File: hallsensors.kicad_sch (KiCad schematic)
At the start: 23 parts

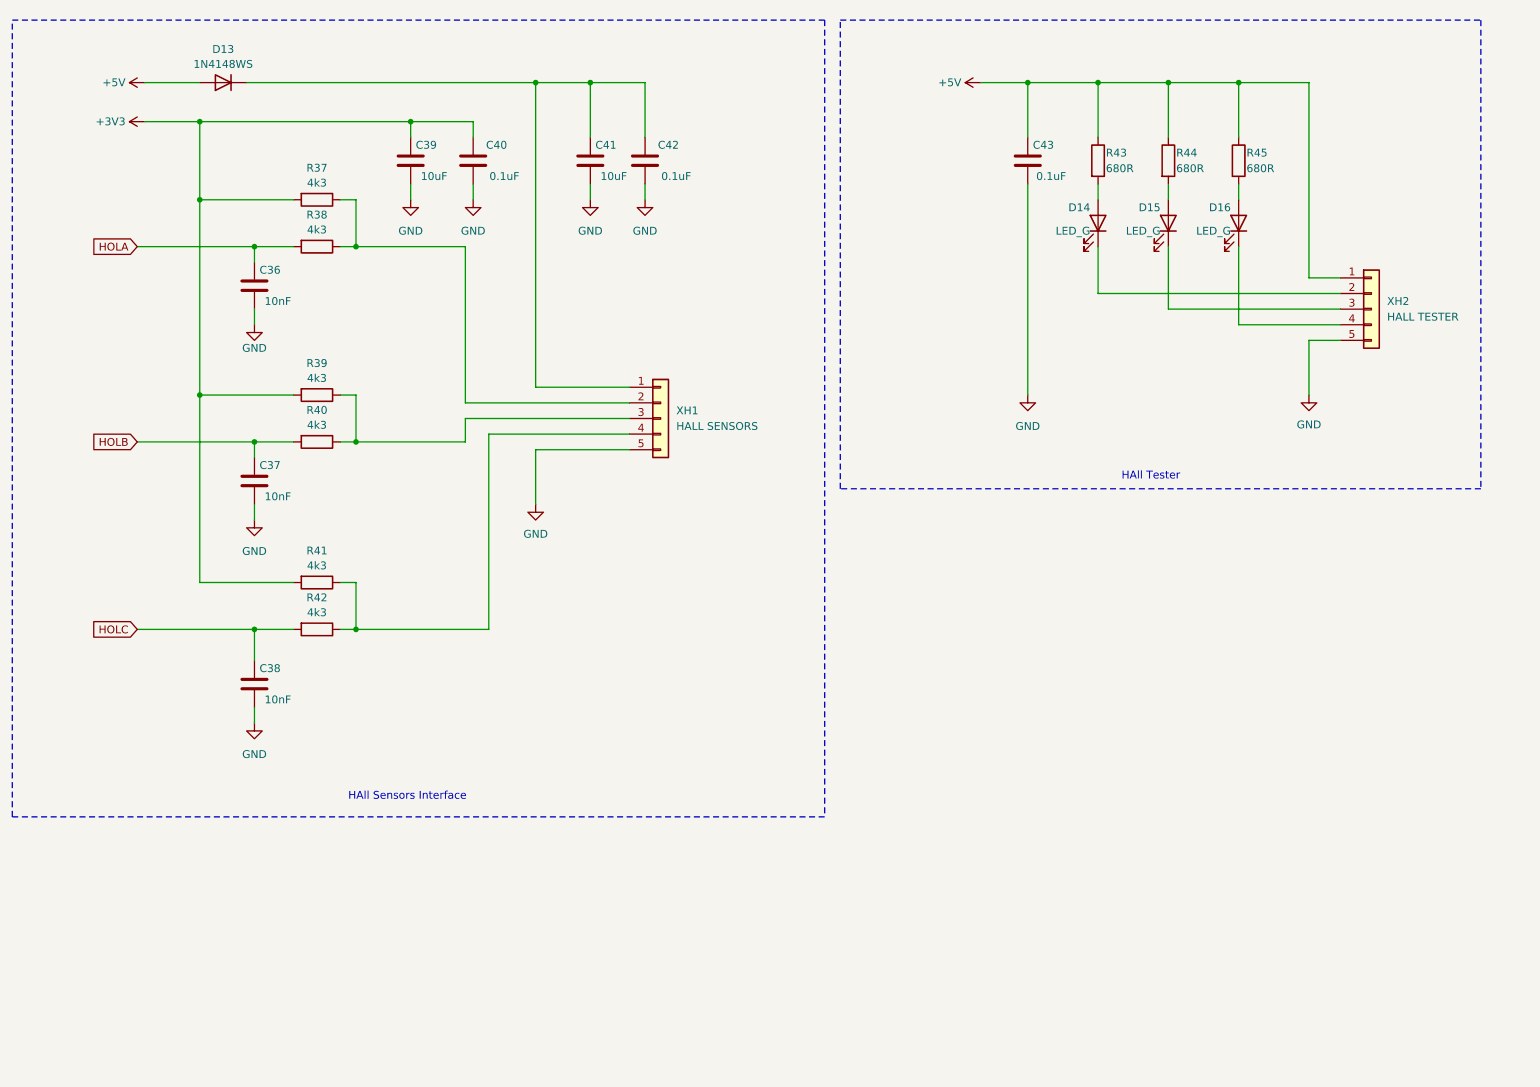
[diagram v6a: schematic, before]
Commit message: Add drivers, stepdown on VIPER115, fixes
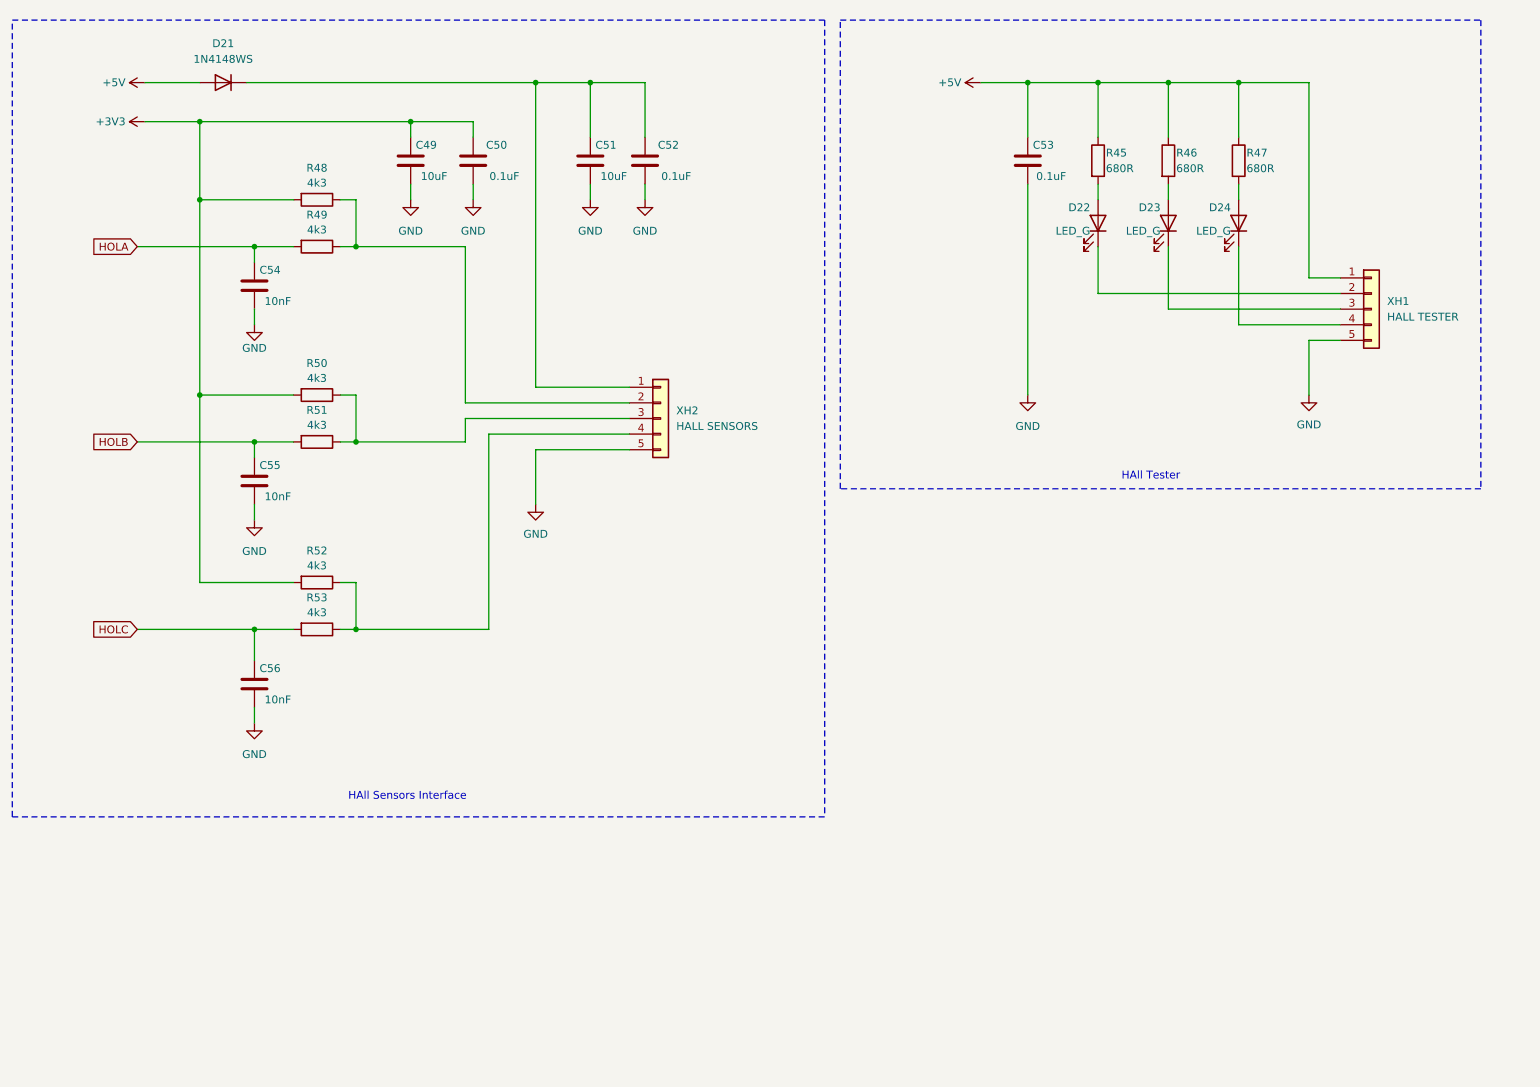
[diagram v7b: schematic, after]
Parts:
- removed D13: 1N4148WS, Diode_SMD:D_SOD-323, symbol Diode:1N4148WS
- added D21: 1N4148WS, Diode_SMD:D_SOD-323, symbol Diode:1N4148WS
- renumbered C39 to C49, C40 to C50, C41 to C51, C42 to C52, C43 to C53, C36 to C54, C37 to C55, C38 to C56, D14 to D22, D15 to D23, D16 to D24, R43 to R45, R44 to R46, R45 to R47, R37 to R48, R38 to R49, R39 to R50, R40 to R51, R41 to R52, R42 to R53, XH2 to XH1, XH1 to XH2
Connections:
- net +5V: now also D21.2 (A)
- net at C51.1, C52.1, XH2.1 (Pin_1): now also D21.1 (K)

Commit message: topology in progress
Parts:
- removed XH1: HALL TESTER, symbol Connector_Generic:Conn_01x05
- removed XH2: HALL SENSORS, symbol Connector_Generic:Conn_01x05
- added XH1: Hall Sensors, Connector_Molex:Molex_Micro-Fit_3.0_43045-0600_2x03_P3.00mm_Horizontal, symbol Connector_Generic:Conn_02x03_Top_Bottom
- added XH2: Hall Tester, Connector_Molex:Molex_Micro-Fit_3.0_43045-0600_2x03_P3.00mm_Horizontal, symbol Connector_Generic:Conn_02x03_Top_Bottom
- D22: value LED_G -> HALL_A
- D23: value LED_G -> HALL_B
- D24: value LED_G -> HALL_C
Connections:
- net +5V: now also XH2.4 (Pin_4)
- net GND: now also XH1.6 (Pin_6), XH2.6 (Pin_6)
- net at D24.1 (K): now also XH2.3 (Pin_3)
- net at R48.1, R49.1: now also XH1.1 (Pin_1)
- net at D22.1 (K): now also XH2.1 (Pin_1)
- net at D23.1 (K): now also XH2.2 (Pin_2)
- net at R52.1, R53.1: now also XH1.3 (Pin_3)
- net at C51.1, C52.1, D21.1 (K): now also XH1.4 (Pin_4)
- net at R50.1, R51.1: now also XH1.2 (Pin_2)
- no-connect marks 0 -> 2
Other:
- note added: "Place for thermistor"
